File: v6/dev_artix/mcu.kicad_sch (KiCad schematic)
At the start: 22 parts, among them J2 Conn_01x04, J3 USB-C Receptable (16P), U11 RPi Pico

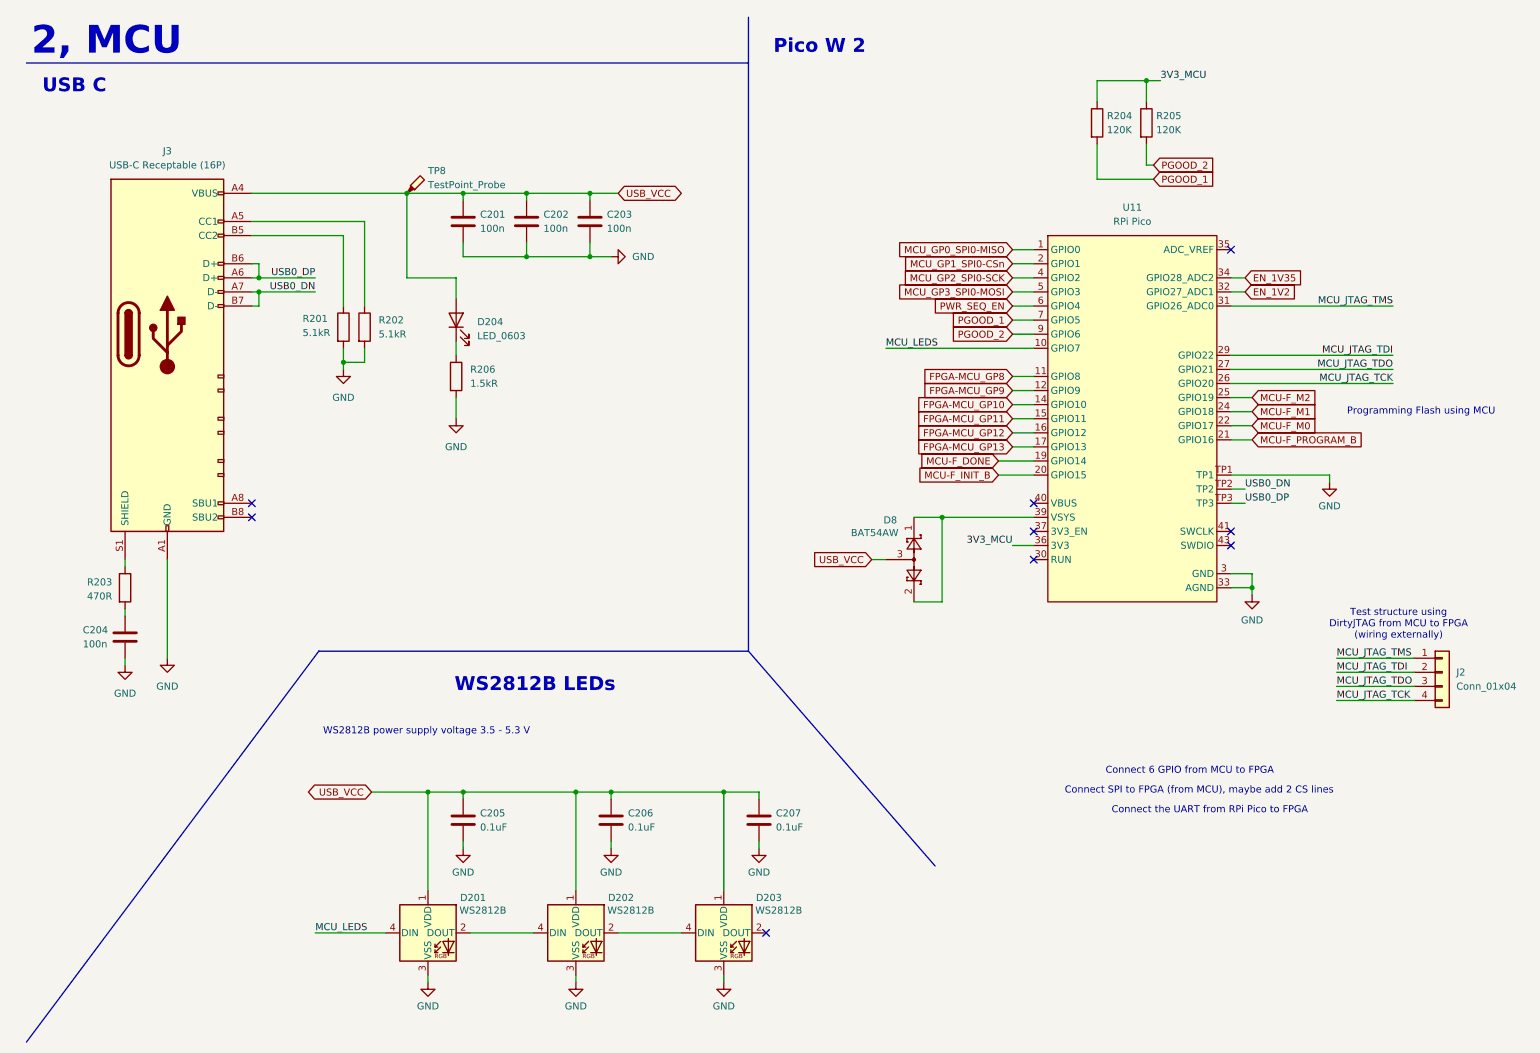
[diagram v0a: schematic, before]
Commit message: Adapt numbers for easier ordering and assembling
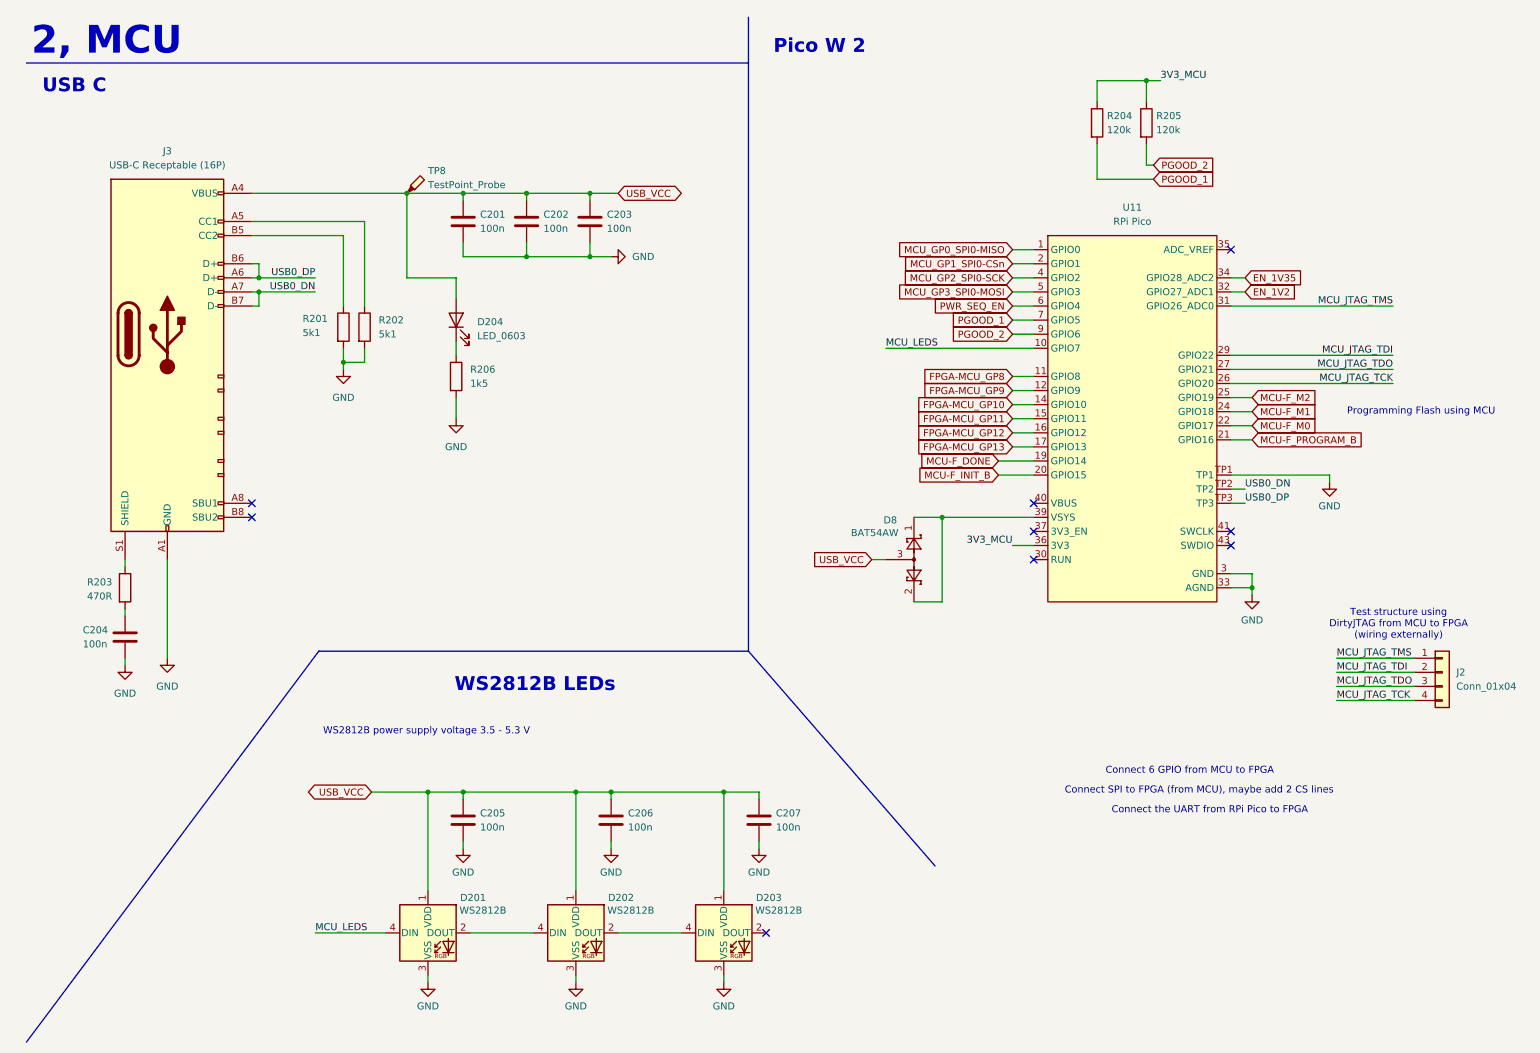
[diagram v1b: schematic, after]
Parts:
- C205, C206, C207: value 0.1uF -> 100n
- R201, R202: value 5.1kR -> 5k1
- R204, R205: value 120K -> 120k
- R206: value 1.5kR -> 1k5
- TP8: now left out of the parts list
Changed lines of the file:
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@@
 			)
 		)
-		(property "Value" "1.5kR"
+		(property "Value" "1k5"
 			(at 92.71 78.7399 0)
 			(effects
@@
 		(unit 1)
 		(exclude_from_sim no)
-		(in_bom yes)
+		(in_bom no)
 		(on_board yes)
 		(dnp no)
@@
 			)
 		)
-		(property "Value" "5.1kR"
+		(property "Value" "5k1"
 			(at 62.484 69.596 0)
 			(effects
@@
 			)
 		)
-		(property "Value" "5.1kR"
+		(property "Value" "5k1"
 			(at 76.2 69.8499 0)
 			(effects
@@
 			)
 		)
-		(property "Value" "0.1uF"
+		(property "Value" "100n"
 			(at 94.488 158.75 0)
 			(effects
@@
 			)
 		)
-		(property "Value" "0.1uF"
+		(property "Value" "100n"
 			(at 147.828 158.75 0)
 			(effects
@@
 			)
 		)
-		(property "Value" "0.1uF"
+		(property "Value" "100n"
 			(at 121.158 158.75 0)
 			(effects
@@
 			)
 		)
-		(property "Value" "120K"
+		(property "Value" "120k"
 			(at 207.518 33.02 0)
 			(effects
@@
 			)
 		)
-		(property "Value" "120K"
+		(property "Value" "120k"
 			(at 216.408 33.02 0)
 			(effects
